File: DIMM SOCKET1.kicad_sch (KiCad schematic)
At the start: 3 parts, among them J5 DIMM REF

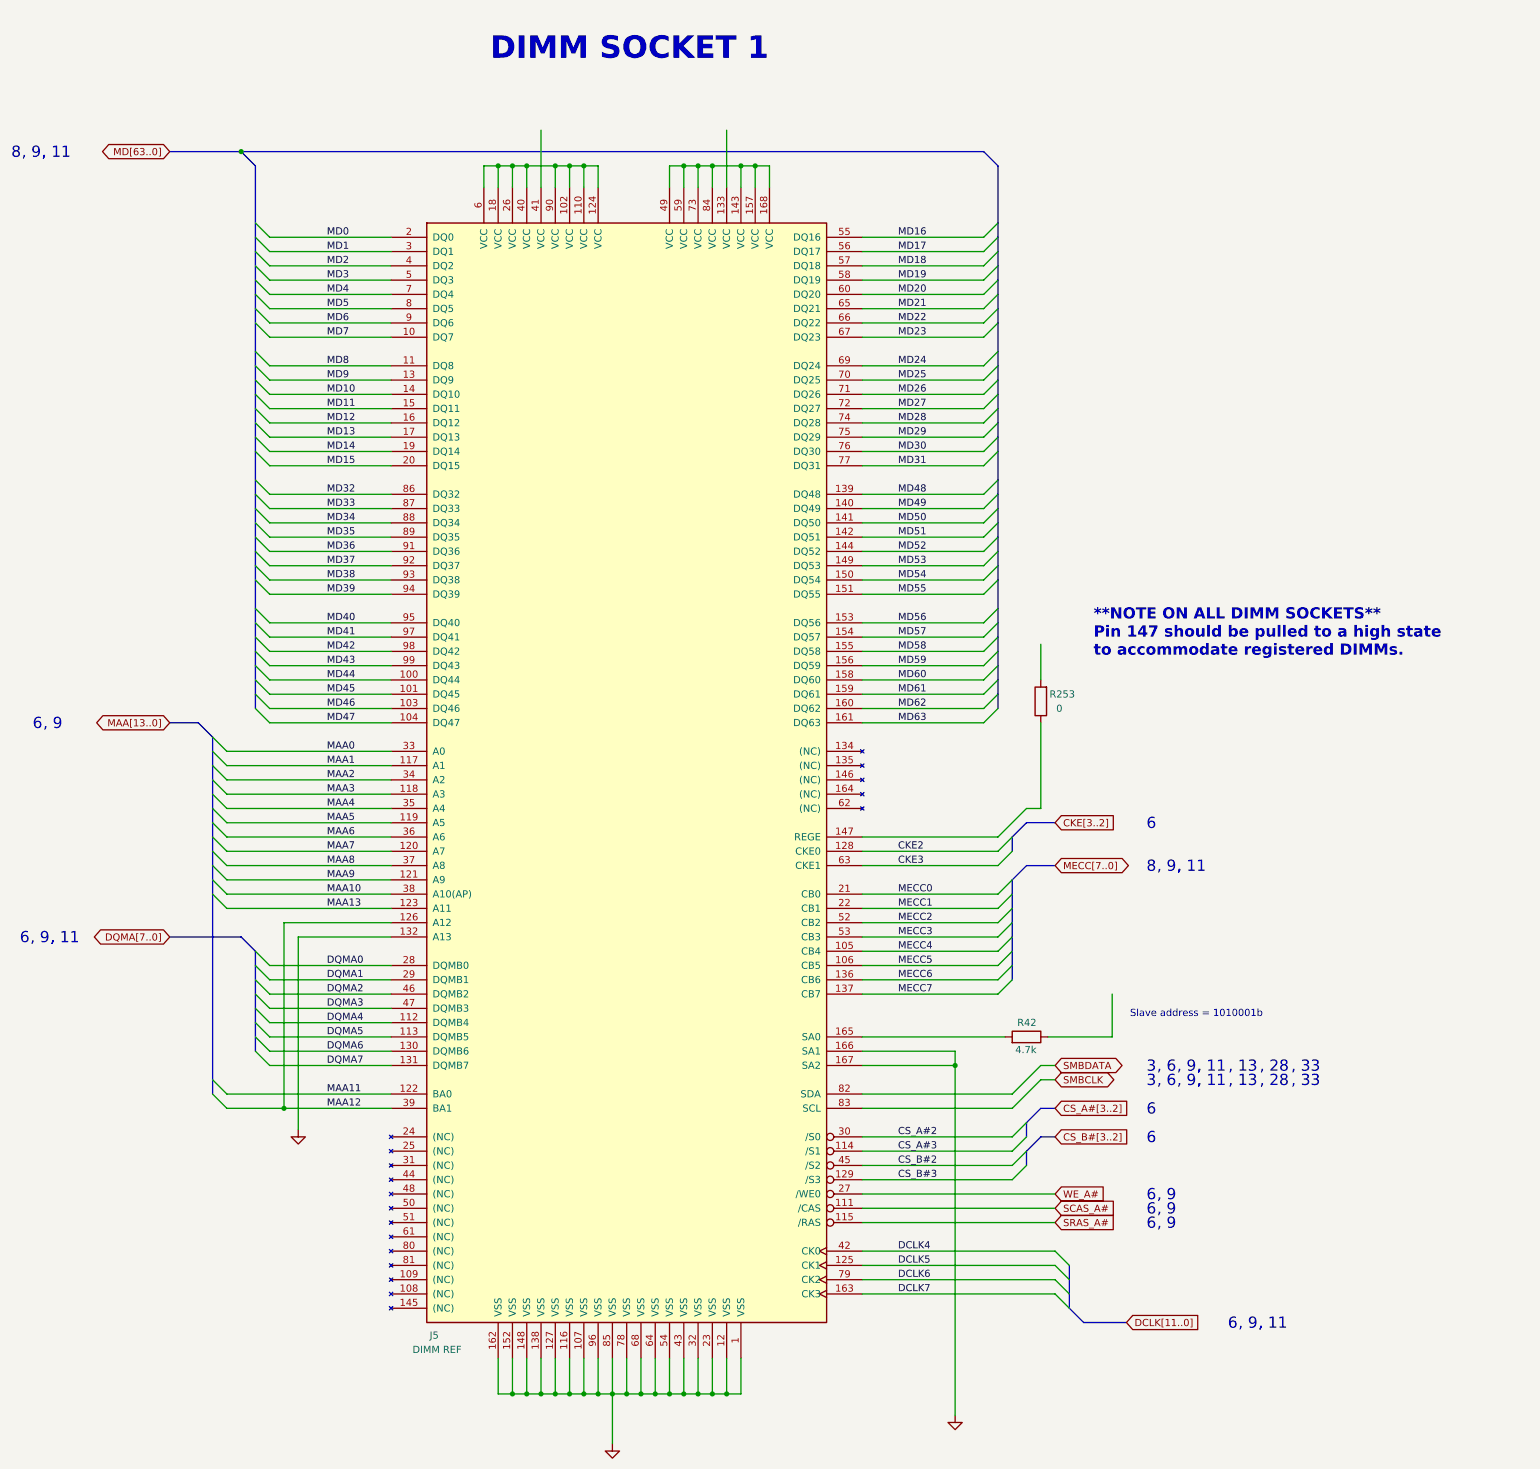
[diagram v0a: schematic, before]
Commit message: page 18 ISA, small fixes
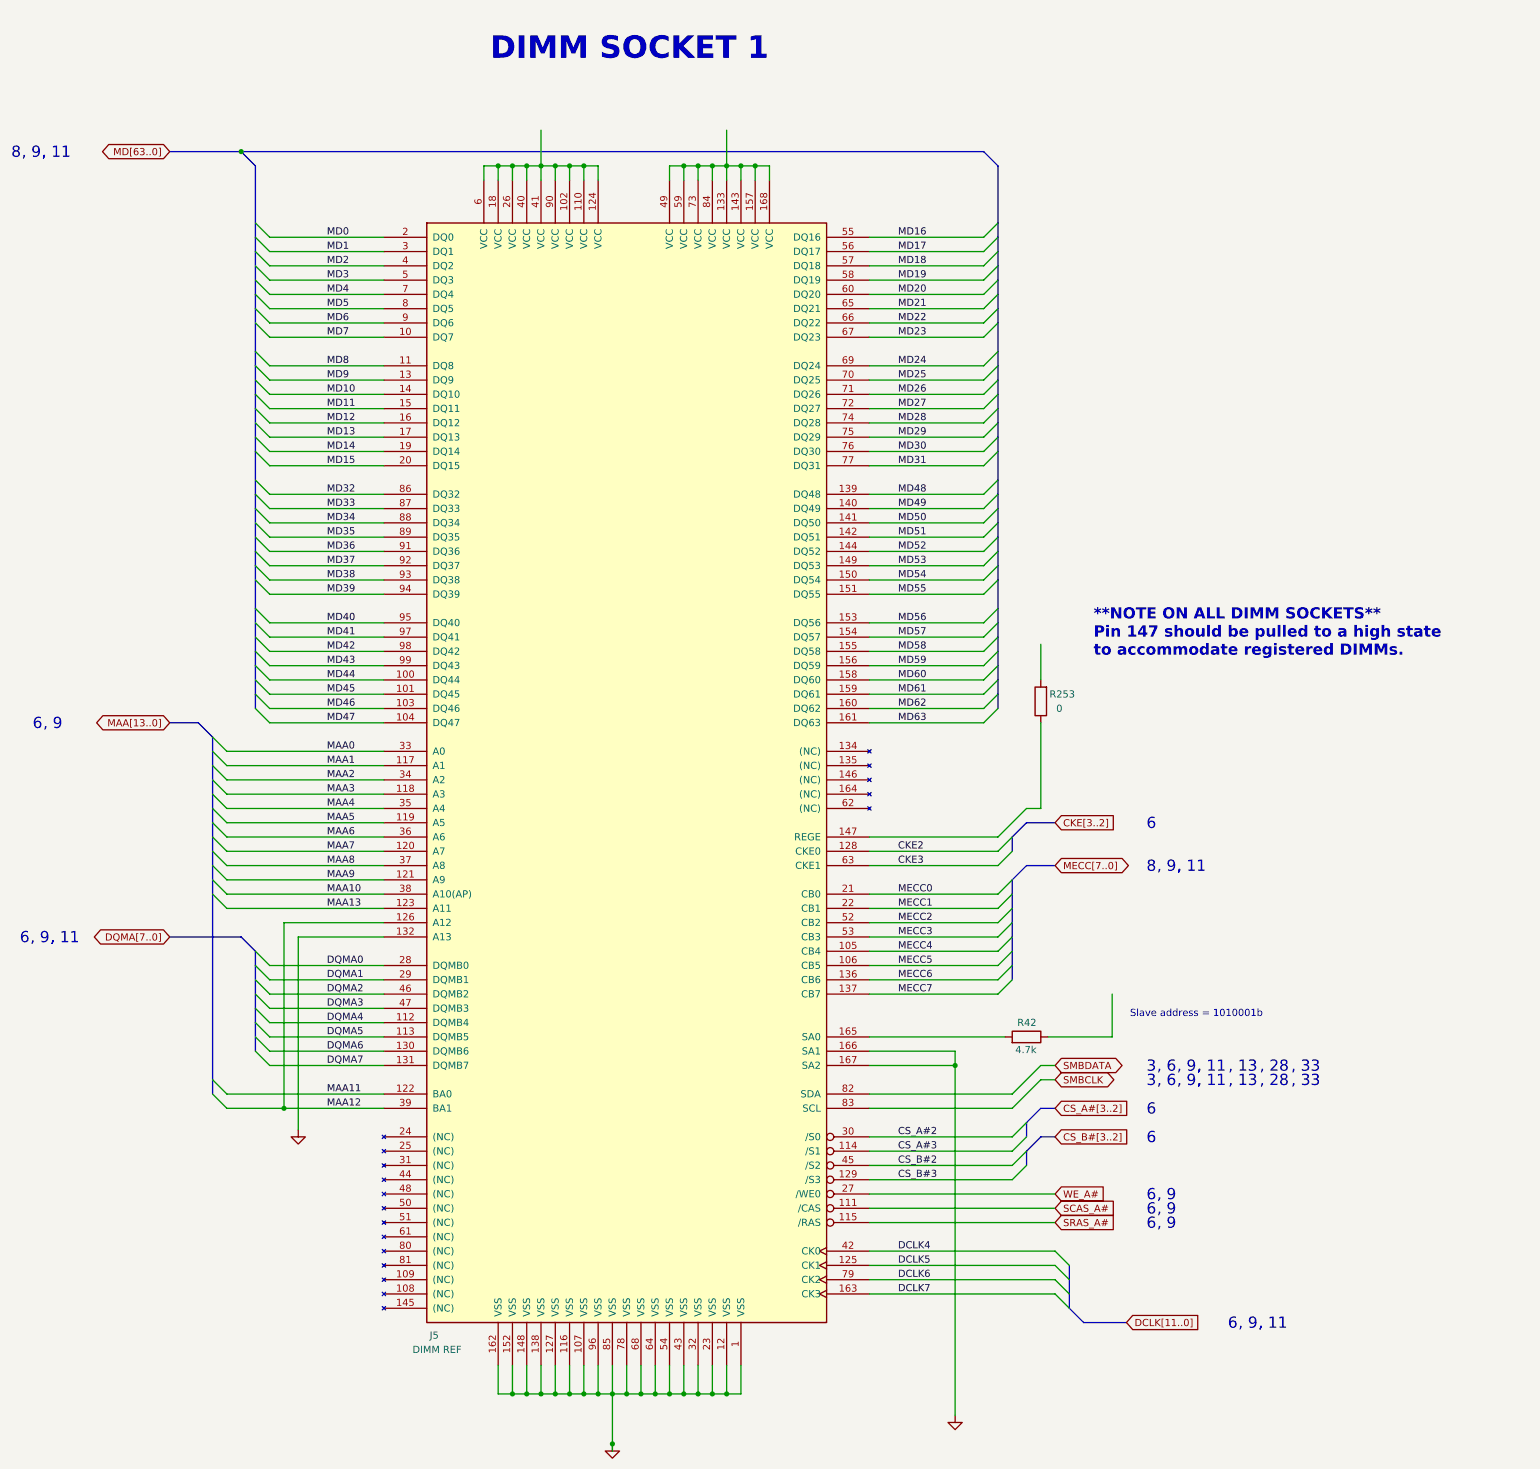
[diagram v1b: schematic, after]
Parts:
- J5: symbol P2-3_era:SDRAM_GENERIC -> P2-3_era:SDRAM_Slot
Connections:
- net at J5.102 (VCC), J5.110 (VCC), J5.124 (VCC)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: now also J5.41 (VCC)
- net at J5.133 (VCC): now also J5.143 (VCC), J5.157 (VCC), J5.168 (VCC), J5.49 (VCC), J5.59 (VCC), J5.73 (VCC), J5.84 (VCC)

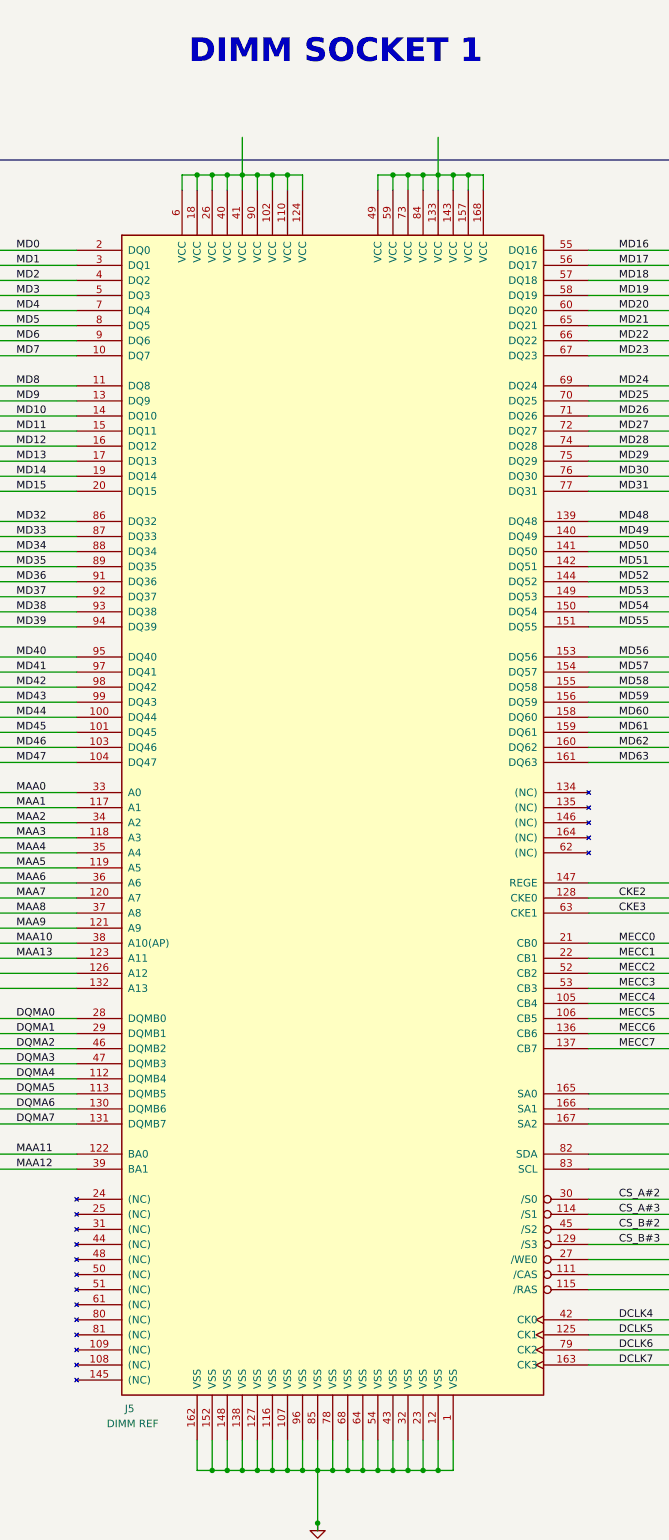
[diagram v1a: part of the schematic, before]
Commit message: page 6,7,8 82443BX chipset, various small fixes
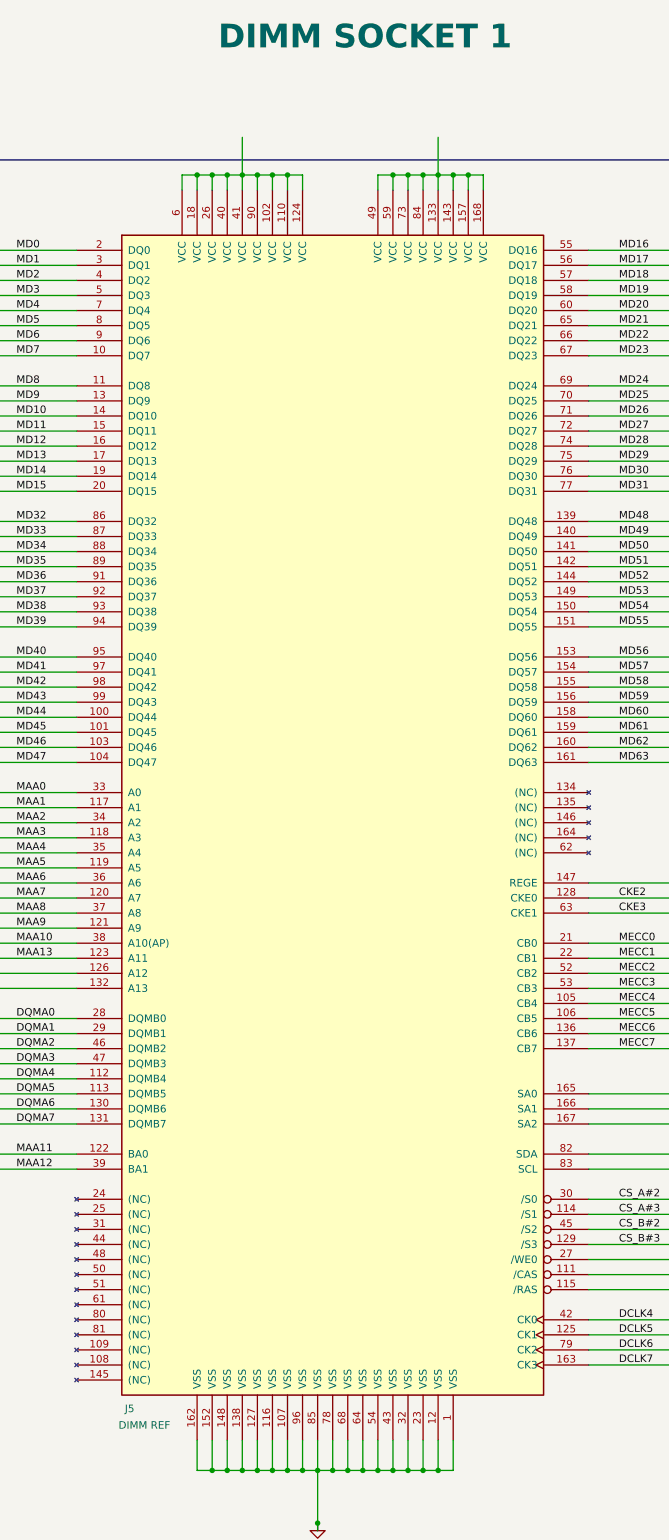
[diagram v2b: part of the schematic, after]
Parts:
- J5: value DIMM REF -> DIMM SOCKET 1
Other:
- note removed: "DIMM SOCKET 1"
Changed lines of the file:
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@@
 		)
 	)
-	(text "DIMM SOCKET 1"
-		(exclude_from_sim no)
-		(at 183.388 29.972 0)
-		(effects
-			(font
-				(size 4 4)
-				(thickness 0.8)
-				(bold yes)
-				(color 0 0 0 1)
-			)
-		)
-	)
 	(text "33"
 		(exclude_from_sim no)
@@
 			)
 		)
-		(property "Value" "DIMM REF"
-			(at 144.78 261.366 0)
+		(property "Value" "DIMM SOCKET 1"
+			(at 163.576 27.432 0)
 			(effects
 				(font
-					(size 1.27 1.27)
+					(size 4 4)
+					(thickness 1)
+					(bold yes)
 				)
 				(justify left)
@@
 			)
 		)
-		(property "Description" "DIMM SOCKET"
-			(at 184.658 186.69 0)
+		(property "Description" "DIMM REF"
+			(at 151.13 261.62 0)
 			(effects
 				(font
 					(size 1.27 1.27)
 				)
-				(hide yes)
 			)
 		)
